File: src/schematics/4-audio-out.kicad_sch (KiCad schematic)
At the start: 26 parts, among them U2 IS31AP4991A-SLS2, U4 MCP6486U, U5 AP22653AW6

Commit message: Finished drawing up the audio output schematic.  The speaker selection is still to do.
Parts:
- removed C66: 4.7μF, restall-generic-capacitors:unpolarised-nominal-0402-1005, symbol restall-generic-capacitors:capacitor-unpolarised
- added C401, C402: 4.7μF, restall-generic-capacitors:unpolarised-nominal-0402-1005, symbol restall-generic-capacitors:capacitor-unpolarised
- added C403, C406: 22μF, restall-generic-capacitors:unpolarised-nominal-0805-2012, symbol restall-generic-capacitors:capacitor-unpolarised
- added C407: DNP, restall-generic-capacitors:unpolarised-nominal-0805-2012, symbol restall-generic-capacitors:capacitor-unpolarised
- added R402: 33kΩ, restall-generic-resistors:nominal-0402-1005, symbol restall-generic-resistors:resistor
- renumbered C64 to C404, C65 to C405, C31 to C408, C32 to C409, C33 to C410, C34 to C411, C26 to C412, C36 to C413, C25 to C414, C27 to C415, C35 to C416, C24 to C417, D8 to D401, FB3 to FB401, R22 to R401, R25 to R403, R29 to R404, R30 to R405, R31 to R406, R32 to R407, R23 to R408, R24 to R409, U5 to U401, U4 to U402, U2 to U403
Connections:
- net AMP_EN: now also U401.3 (EN), R402.1; no longer U403.1 (SDB)
- net AUDIO_AMP_{+5V}: now also C401.1
- net AUDIO_VDD_{+5V}: now also U403.1 (SDB), C406.1, C407.1
- net GND: now also C401.2, C402.2, C403.2, C406.2, C407.2
- net ~{AMP_FAULT}: now reaches U401.4 (~{FAULT})
- net ~{AMP_FAULT}: now also R402.2
- net at FB401.1 (P1), U401.6 (OUT): now also C402.1, C403.1
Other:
- note removed: "TODO: BYPASS CAPS FOR INPUT AND OUTPUT OF AP22653AW6"
- note removed: "TODO: FOR AUDIO_AMP_{+5V} - KEEP C_{EFF} < 90uF (see 1-usb) !"
- note removed: "TODO: WHAT TO DO WITH ~{FAULT} ? WOULD BE NICE TO TIE TO THE 'EN' PIN AS OPEN-DRAIN BUT THAT WILL PROBABLY OSCILLATE"
- moved on the sheet: C404, C405, C408, C409, C410, C411, C412, C413, C414, C415, C416, C417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

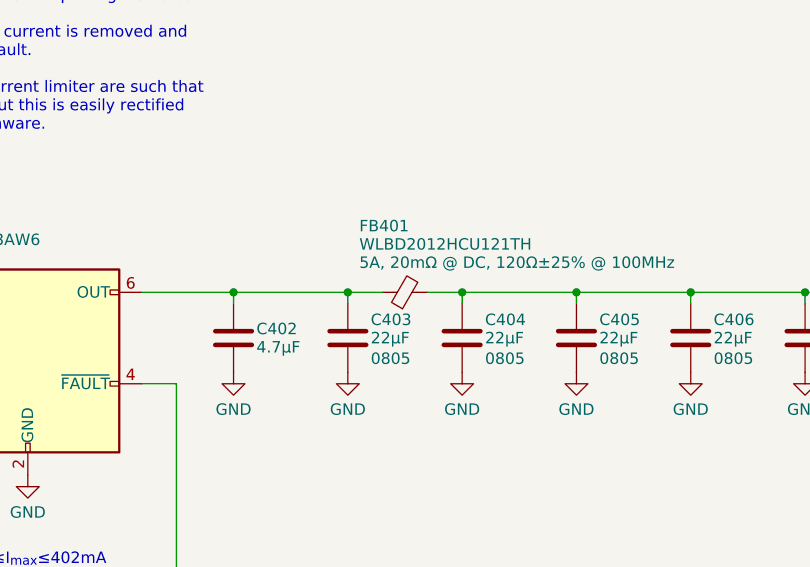
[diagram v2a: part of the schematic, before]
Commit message: Drew the schematic for the TFT driver.
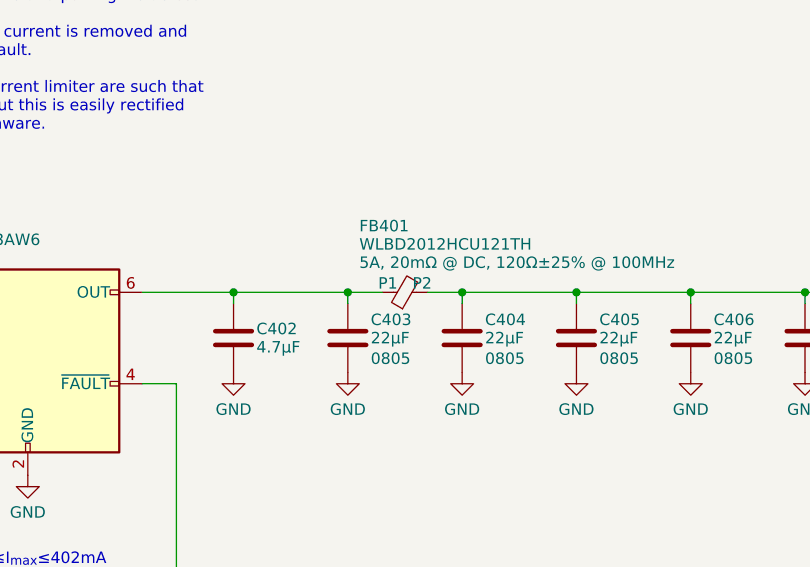
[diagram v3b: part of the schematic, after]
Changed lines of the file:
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@@
     )
   )
-  (symbol (lib_name "MCP6486U?-?-?T_1") (lib_id "restall-manufacturer-microchip:MCP6486U?-?-?T") (at 199.39 152.4 0) (mirror x) (unit 1)
+  (symbol (lib_id "restall-manufacturer-microchip:MCP6486U?-?-?T") (at 199.39 152.4 0) (mirror x) (unit 1)
     (in_bom yes) (on_board yes) (dnp no)
     (property "Reference" "U402" (at 199.39 158.75 0)
@@
     )
   )
-  (symbol (lib_name "IS31AP4991A-?LS2_1") (lib_id "restall-manufacturer-lumissil:IS31AP4991A-?LS2") (at 245.11 157.48 0) (unit 1)
+  (symbol (lib_id "restall-manufacturer-lumissil:IS31AP4991A-?LS2") (at 245.11 157.48 0) (unit 1)
     (in_bom yes) (on_board yes) (dnp no)
     (property "Reference" "U403" (at 244.348 164.084 0)

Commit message: Further elaboration of the circuitry surrounding the microcontroller.
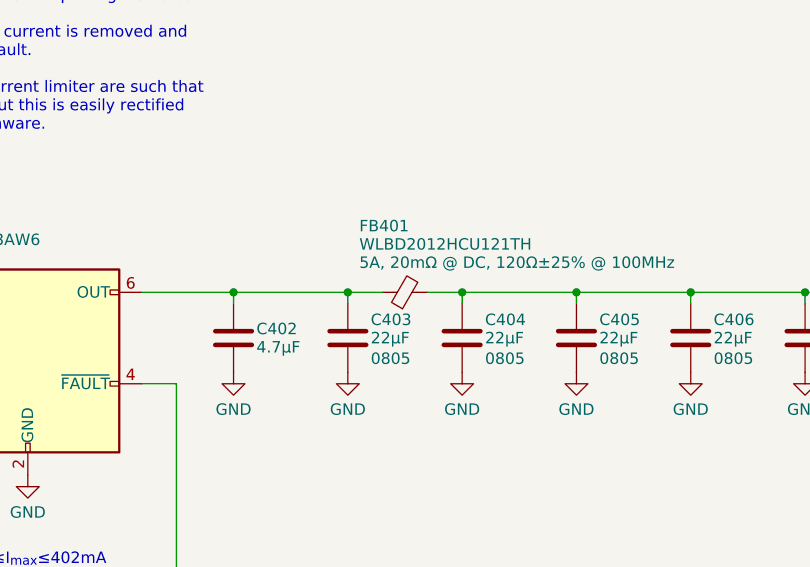
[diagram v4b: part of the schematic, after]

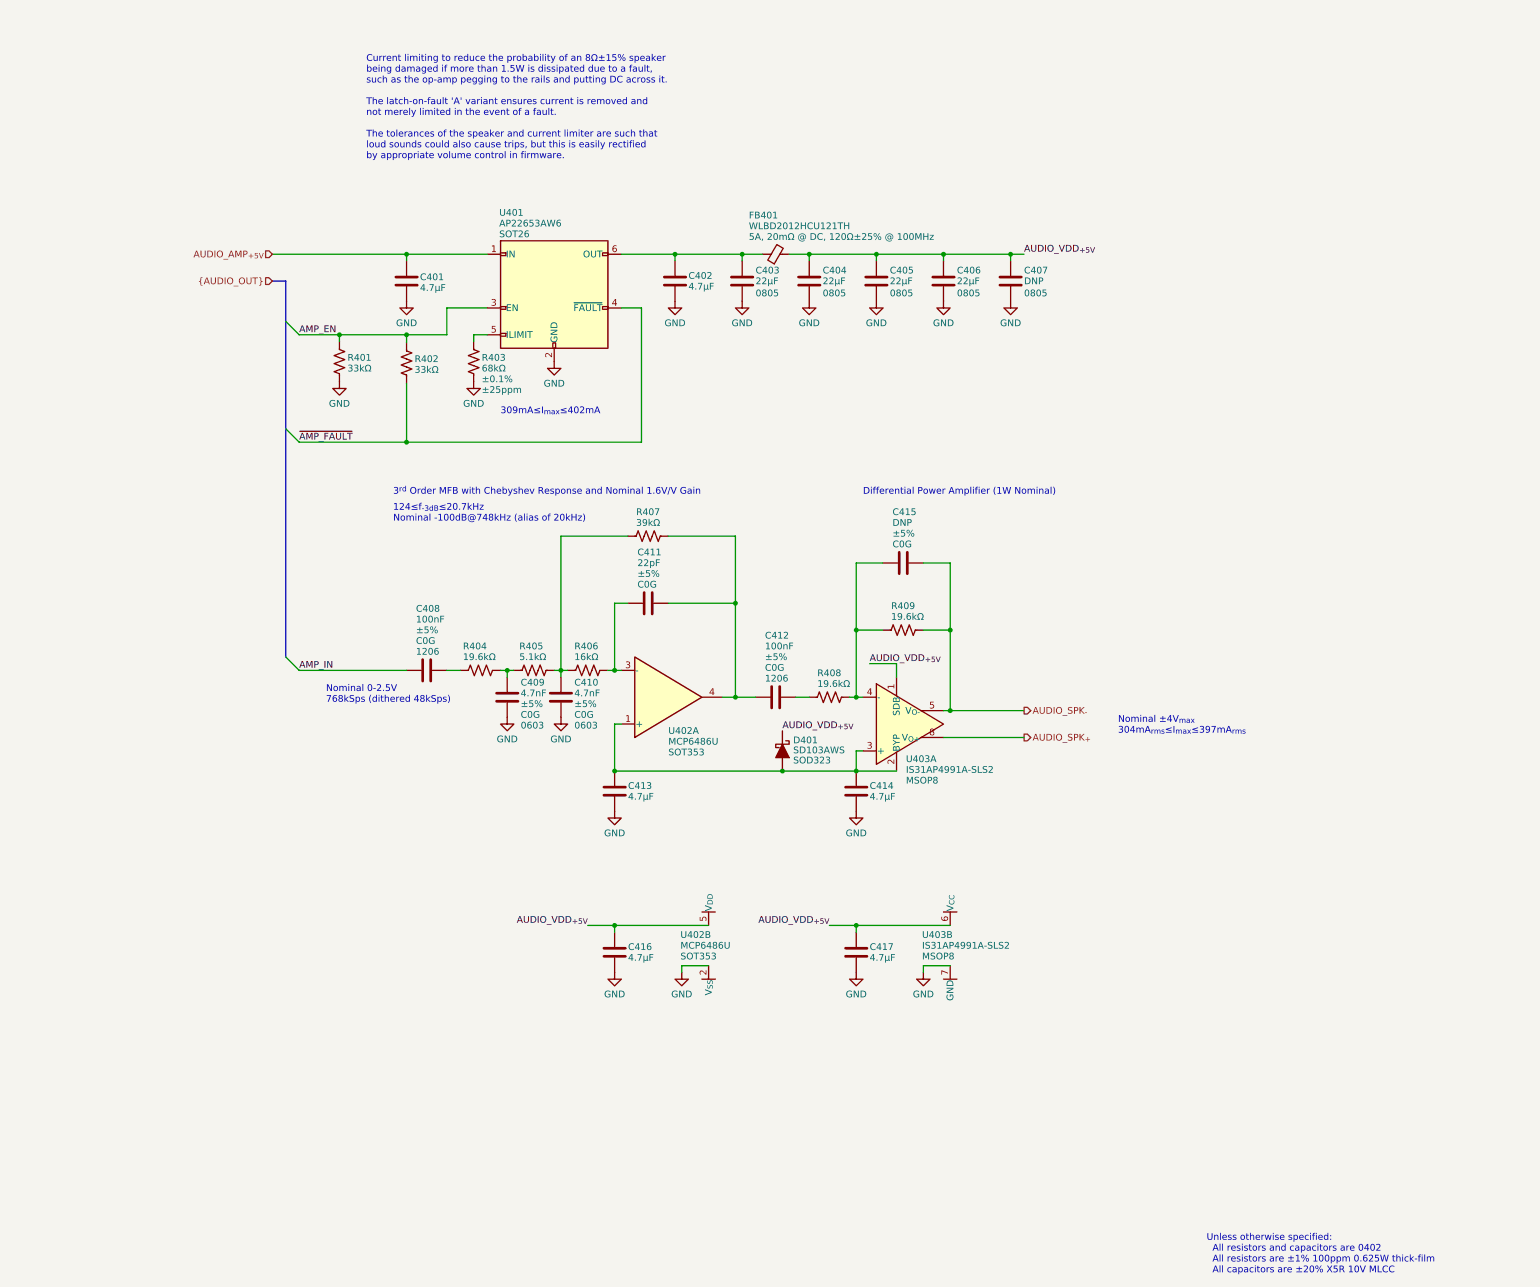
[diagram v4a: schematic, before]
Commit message: Various tidy-ups and checks, mainly around the bypass capacitors.  Added a load of test points.
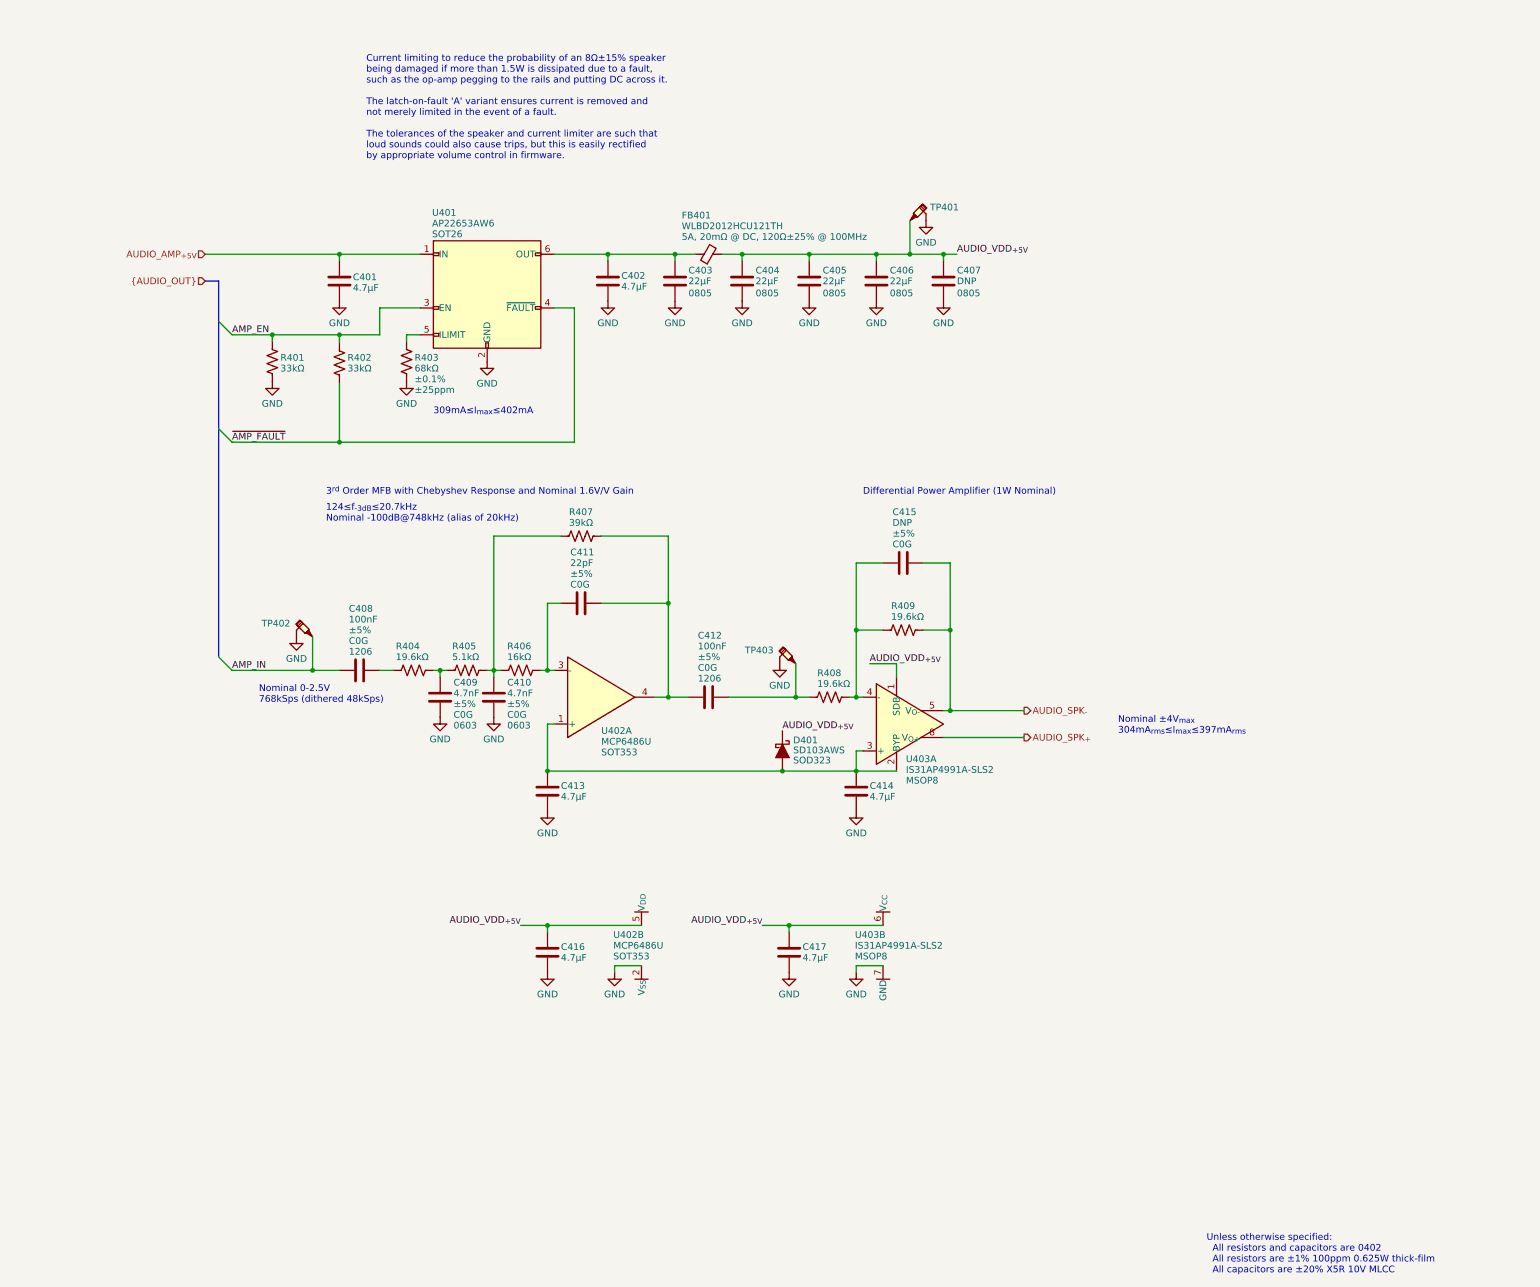
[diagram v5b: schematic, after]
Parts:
- added TP401, TP402, TP403: ~, restall-generic-test:testpoint-SP3050A-with-short-gnd, symbol restall-generic-test:testpoint-probe-with-gnd
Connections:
- net AMP_IN: now also TP402.1
- net AUDIO_VDD_{+5V}: now also TP401.1
- net GND: now also TP401.2 (GND), TP402.2 (GND), TP403.2 (GND)
- net at C412.2, R408.1: now also TP403.1
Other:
- moved on the sheet: C401, C402, C403, C404, C405, C406, C407, C408, C409, C410, C411, C412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

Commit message: Added part numbers for the capacitors.
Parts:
- C401, C402, C413, C414, C416, C417: ManufacturerPartNumber (none) -> CL05A475MP5NRNC
- C411: Manufacturer (none) -> Murata; Manufacturer2 (none) -> Murata; Manufacturer2PartNumber (none) -> GCM1555C1H220GA16D; ManufacturerPartNumber (none) -> GCM1555C1H220FA16D
- FB401: Package (none) -> WLBD2012
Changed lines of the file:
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@@
       (effects (font (size 1.27 1.27)) (justify left) hide)
     )
-    (property "ManufacturerPartNumber" "" (at 187.96 73.66 0)
+    (property "ManufacturerPartNumber" "CL05A475MP5NRNC" (at 187.96 73.66 0)
       (effects (font (size 1.27 1.27)) (justify left) hide)
     )
@@
       (effects (font (size 1.27 1.27)) (justify right) hide)
     )
-    (property "Manufacturer" "" (at 182.88 134.62 0)
-      (effects (font (size 1.27 1.27)) (justify left) hide)
-    )
-    (property "ManufacturerPartNumber" "" (at 182.88 134.62 0)
-      (effects (font (size 1.27 1.27)) (justify left) hide)
-    )
-    (property "Manufacturer2" "" (at 182.88 134.62 0)
-      (effects (font (size 1.27 1.27)) (justify left) hide)
-    )
-    (property "Manufacturer2PartNumber" "" (at 182.88 134.62 0)
+    (property "Manufacturer" "Murata" (at 182.88 134.62 0)
+      (effects (font (size 1.27 1.27)) (justify left) hide)
+    )
+    (property "ManufacturerPartNumber" "GCM1555C1H220FA16D" (at 182.88 134.62 0)
+      (effects (font (size 1.27 1.27)) (justify left) hide)
+    )
+    (property "Manufacturer2" "Murata" (at 182.88 134.62 0)
+      (effects (font (size 1.27 1.27)) (justify left) hide)
+    )
+    (property "Manufacturer2PartNumber" "GCM1555C1H220GA16D" (at 182.88 134.62 0)
       (effects (font (size 1.27 1.27)) (justify left) hide)
     )
@@
       (effects (font (size 1.27 1.27)) (justify left) hide)
     )
-    (property "ManufacturerPartNumber" "" (at 176.53 200.66 0)
+    (property "ManufacturerPartNumber" "CL05A475MP5NRNC" (at 176.53 200.66 0)
       (effects (font (size 1.27 1.27)) (justify left) hide)
     )
@@
       (effects (font (size 1.27 1.27)) (justify left) hide)
     )
-    (property "ManufacturerPartNumber" "" (at 222.25 200.66 0)
+    (property "ManufacturerPartNumber" "CL05A475MP5NRNC" (at 222.25 200.66 0)
       (effects (font (size 1.27 1.27)) (justify left) hide)
     )
@@
       (effects (font (size 1.27 1.27)) (justify left) hide)
     )
-    (property "ManufacturerPartNumber" "" (at 234.95 170.18 0)
+    (property "ManufacturerPartNumber" "CL05A475MP5NRNC" (at 234.95 170.18 0)
       (effects (font (size 1.27 1.27)) (justify left) hide)
     )
@@
       (effects (font (size 1.27 1.27)) (justify left) hide)
     )
+    (property "Package" "WLBD2012" (at 207.01 68.58 0)
+      (effects (font (size 1.27 1.27)) hide)
+    )
     (pin "1")
     (pin "2")
@@
       (effects (font (size 1.27 1.27)) (justify left) hide)
     )
-    (property "ManufacturerPartNumber" "" (at 176.53 170.18 0)
+    (property "ManufacturerPartNumber" "CL05A475MP5NRNC" (at 176.53 170.18 0)
       (effects (font (size 1.27 1.27)) (justify left) hide)
     )
@@
       (effects (font (size 1.27 1.27)) (justify left) hide)
     )
-    (property "ManufacturerPartNumber" "" (at 137.16 73.66 0)
-      (effects (font (size 1.27 1.27)) (justify left) hide)
-    )
+    (property "ManufacturerPartNumber" "CL05A475MP5NRNC" (at 137.16 73.66 0)
+      (effects (font (size 1.27 1.27)) (justify left) hide)
+    )
